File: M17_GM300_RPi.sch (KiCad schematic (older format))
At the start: 37 parts, among them J1 RJ45, J2 SJ1-3523N, J3 1935161, J4 DB9_Female, J5 RPi Header, Q1 2N7000, Q2 2N7000, Q3 2N7000, Q4 2N7000, SW1 SW_Push, U1 LM2576HVS-5, U2 4066, U3 LM386

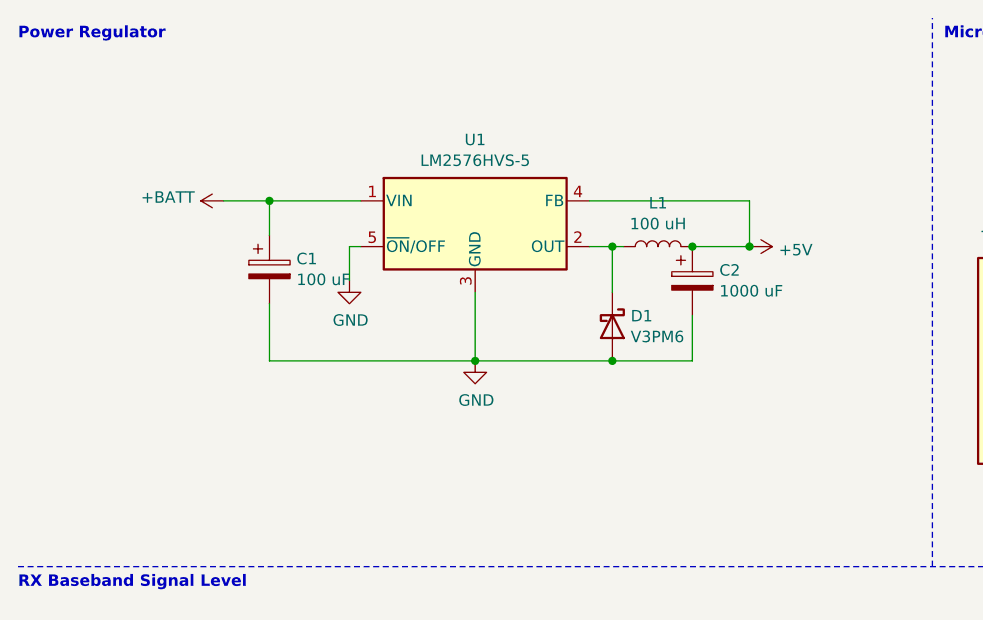
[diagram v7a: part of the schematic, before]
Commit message: Created new symbol and footprint for new power supply; removed old and added new power supply to schem; updated pcb with the changes.
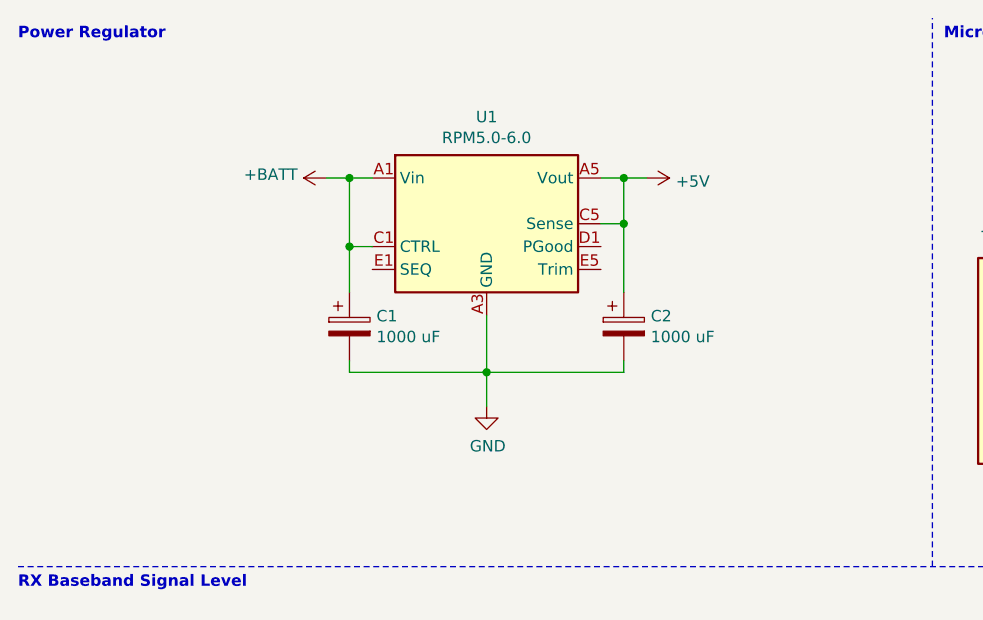
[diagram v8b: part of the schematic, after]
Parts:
- removed D1: V3PM6, symbol Device:D_Schottky
- removed L1: 100 uH, Inductor_SMD:L_0603_1608Metric, symbol Device:L
- removed U1: LM2576HVS-5, Package_TO_SOT_SMD:TO-263-5_TabPin3, symbol Regulator_Switching:LM2576HVS-5
- added U1: RPM5.0-6.0, Power_Supplies:RPM5.0-6.0, symbol Power_Supplies:RPM5.0-6.0
- C1: value 100 uF -> 1000 uF
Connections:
- net +5V: now also U1.A5 (Vout), U1.B5 (Vout), U1.C5 (Sense)
- net +BATT: now also U1.A1 (Vin), U1.A2 (Vin), U1.C1 (CTRL)
- net GND: now also U1.A3 (GND), U1.A4 (GND), U1.B1 (GND), U1.B2 (GND), U1.B3 (GND), U1.B4 (GND), U1.C2 (GND), U1.C3 (GND), U1.C4 (GND), U1.D2 (GND), U1.D3 (GND), U1.D4 (GND), U1.D5 (GND), U1.E3 (GND), U1.E4 (GND)
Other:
- moved on the sheet: C1, C2
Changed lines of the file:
@@
 SPK_MUTE
-$Comp
-L Regulator_Switching:LM2576HVS-5 U1
-U 1 1 60542727
-P 2500 1400
-F 0 "U1" H 2500 1767 50  0000 C CNN
-F 1 "LM2576HVS-5" H 2500 1676 50  0000 C CNN
-F 2 "Package_TO_SOT_SMD:TO-263-5_TabPin3" H 2500 1150 50  0001 L CIN
-F 3 "http://www.ti.com/lit/ds/symlink/lm2576.pdf" H 2500 1400 50  0001 C CNN
-	1    2500 1400
-	1    0    0    -1
-$EndComp
 $Comp
 L power:+BATT #PWR01
 U 1 1 60543972
-P 1400 1300
-F 0 "#PWR01" H 1400 1150 50  0001 C CNN
-F 1 "+BATT" V 1415 1427 50  0000 L CNN
-F 2 "" H 1400 1300 50  0001 C CNN
-F 3 "" H 1400 1300 50  0001 C CNN
-	1    1400 1300
+P 1850 1200
+F 0 "#PWR01" H 1850 1050 50  0001 C CNN
+F 1 "+BATT" V 1865 1327 50  0000 L CNN
+F 2 "" H 1850 1200 50  0001 C CNN
+F 3 "" H 1850 1200 50  0001 C CNN
+	1    1850 1200
 	0    -1   -1   0
 $EndComp
@@
 L power:GND #PWR03
 U 1 1 60543DCC
-P 2500 2000
-F 0 "#PWR03" H 2500 1750 50  0001 C CNN
-F 1 "GND" H 2505 1827 50  0000 C CNN
-F 2 "" H 2500 2000 50  0001 C CNN
-F 3 "" H 2500 2000 50  0001 C CNN
-	1    2500 2000
+P 2550 2200
+F 0 "#PWR03" H 2550 1950 50  0001 C CNN
+F 1 "GND" H 2555 2027 50  0000 C CNN
+F 2 "" H 2550 2200 50  0001 C CNN
+F 3 "" H 2550 2200 50  0001 C CNN
+	1    2550 2200
 	1    0    0    -1
 $EndComp
 $Comp
-L power:GND #PWR02
-U 1 1 605442BC
-P 1950 1650
-F 0 "#PWR02" H 1950 1400 50  0001 C CNN
-F 1 "GND" H 1955 1477 50  0000 C CNN
-F 2 "" H 1950 1650 50  0001 C CNN
-F 3 "" H 1950 1650 50  0001 C CNN
-	1    1950 1650
-	1    0    0    -1
-$EndComp
-Wire Wire Line
-	2000 1500 1950 1500
-Wire Wire Line
-	1950 1500 1950 1650
-Wire Wire Line
-	2500 1700 2500 2000
-$Comp
 L M17_GM300_RPi-rescue:C_Polarized-Device C1
 U 1 1 6054C3EF
-P 1600 1600
-F 0 "C1" H 1718 1646 50  0000 L CNN
-F 1 "100 uF" H 1718 1555 50  0000 L CNN
-F 2 "Capacitor_SMD:C_0603_1608Metric" H 1638 1450 50  0001 C CNN
-F 3 "~" H 1600 1600 50  0001 C CNN
-	1    1600 1600
+P 1950 1850
+F 0 "C1" H 2068 1896 50  0000 L CNN
+F 1 "1000 uF" H 2068 1805 50  0000 L CNN
+F 2 "Capacitor_SMD:C_0603_1608Metric" H 1988 1700 50  0001 C CNN
+F 3 "~" H 1950 1850 50  0001 C CNN
+	1    1950 1850
 	1    0    0    -1
-$EndComp
-$Comp
-L Device:L L1
-U 1 1 6054CA01
-P 3300 1500
-F 0 "L1" V 3490 1500 50  0000 C CNN
-F 1 "100 uH" V 3399 1500 50  0000 C CNN
-F 2 "Inductor_SMD:L_0603_1608Metric" H 3300 1500 50  0001 C CNN
-F 3 "~" H 3300 1500 50  0001 C CNN
-	1    3300 1500
-	0    -1   -1   0
 $EndComp
 $Comp
 L M17_GM300_RPi-rescue:C_Polarized-Device C2
 U 1 1 6054D08D
-P 3450 1650
-F 0 "C2" H 3568 1696 50  0000 L CNN
-F 1 "1000 uF" H 3568 1605 50  0000 L CNN
-F 2 "Capacitor_SMD:C_0603_1608Metric" H 3488 1500 50  0001 C CNN
-F 3 "~" H 3450 1650 50  0001 C CNN
-	1    3450 1650
+P 3150 1850
+F 0 "C2" H 3268 1896 50  0000 L CNN
+F 1 "1000 uF" H 3268 1805 50  0000 L CNN
+F 2 "Capacitor_SMD:C_0603_1608Metric" H 3188 1700 50  0001 C CNN
+F 3 "~" H 3150 1850 50  0001 C CNN
+	1    3150 1850
 	1    0    0    -1
 $EndComp
@@
 L power:+5V #PWR04
 U 1 1 6054D592
-P 3700 1500
-F 0 "#PWR04" H 3700 1350 50  0001 C CNN
-F 1 "+5V" V 3715 1628 50  0000 L CNN
-F 2 "" H 3700 1500 50  0001 C CNN
-F 3 "" H 3700 1500 50  0001 C CNN
-	1    3700 1500
+P 3250 1200
+F 0 "#PWR04" H 3250 1050 50  0001 C CNN
+F 1 "+5V" V 3265 1328 50  0000 L CNN
+F 2 "" H 3250 1200 50  0001 C CNN
+F 3 "" H 3250 1200 50  0001 C CNN
+	1    3250 1200
 	0    1    1    0
 $EndComp
-Wire Wire Line
-	3000 1300 3700 1300
-Wire Wire Line
-	3700 1300 3700 1500
-Connection ~ 2500 2000
-Wire Wire Line
-	3100 2000 2500 2000
-Wire Wire Line
-	3450 1500 3700 1500
-Connection ~ 3450 1500
-Connection ~ 3700 1500
-Wire Wire Line
-	1600 1750 1600 2000
-Wire Wire Line
-	1600 2000 2500 2000
-Wire Wire Line
-	1400 1300 1600 1300
-Wire Wire Line
-	1600 1300 1600 1450
-Connection ~ 1600 1300
-Wire Wire Line
-	1600 1300 2000 1300
 $Comp
-L Device:D_Schottky D1
-U 1 1 6055A4E3
-P 3100 1850
-F 0 "D1" V 3054 1930 50  0000 L CNN
-F 1 "V3PM6" V 3145 1930 50  0000 L CNN
-F 2 "" H 3100 1850 50  0001 C CNN
-F 3 "~" H 3100 1850 50  0001 C CNN
-	1    3100 1850
-	0    1    1    0
+L Power_Supplies:RPM5.0-6.0 U1
+U 1 1 606BCADF
+P 2550 1400
+F 0 "U1" H 2550 1867 50  0000 C CNN
+F 1 "RPM5.0-6.0" H 2550 1776 50  0000 C CNN
+F 2 "Power_Supplies:RPM5.0-6.0" H 2650 1900 50  0001 C CNN
+F 3 "https://www.recom-power.com/pdf/Innoline/RPM-6.0.pdf" H 2650 1900 50  0001 C CNN
+	1    2550 1400
+	1    0    0    -1
 $EndComp
 Wire Wire Line
-	3000 1500 3100 1500
+	3250 1200 3150 1200
 Wire Wire Line
-	3100 1700 3100 1500
-Connection ~ 3100 1500
+	3150 1700 3150 1400
+Connection ~ 3150 1200
 Wire Wire Line
-	3100 1500 3150 1500
+	3150 1200 3050 1200
 Wire Wire Line
-	3450 1800 3450 2000
+	1850 1200 1950 1200
 Wire Wire Line
-	3450 2000 3100 2000
-Connection ~ 3100 2000
+	1950 1700 1950 1500
+Connection ~ 1950 1200
+Wire Wire Line
+	1950 1200 2050 1200
+Wire Wire Line
+	1950 2000 1950 2050
+Wire Wire Line
+	1950 2050 2550 2050
+Wire Wire Line
+	3150 2050 3150 2000
+Connection ~ 2550 2050
+Wire Wire Line
+	2550 2050 3150 2050
+Wire Wire Line
+	2550 2050 2550 1800
+Wire Wire Line
+	2550 2050 2550 2200
+Wire Wire Line
+	2050 1500 1950 1500
+Connection ~ 1950 1500
+Wire Wire Line
+	1950 1500 1950 1200
+Wire Wire Line
+	3050 1400 3150 1400
+Connection ~ 3150 1400
+Wire Wire Line
+	3150 1400 3150 1200
 $EndSCHEMATC
